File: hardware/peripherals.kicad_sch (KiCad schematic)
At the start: 32 parts, among them J6 PCM12SMTR, J7 USB_C_Receptacle_USB2.0_14P, J8 BM03B-SRSS-TB, Q4 2N7002, SW1 SW_Push, U3 74AHCT1G125, U4 DS3231MZ, U5 USBLC6-2SC6, U6 74AHCT1G32

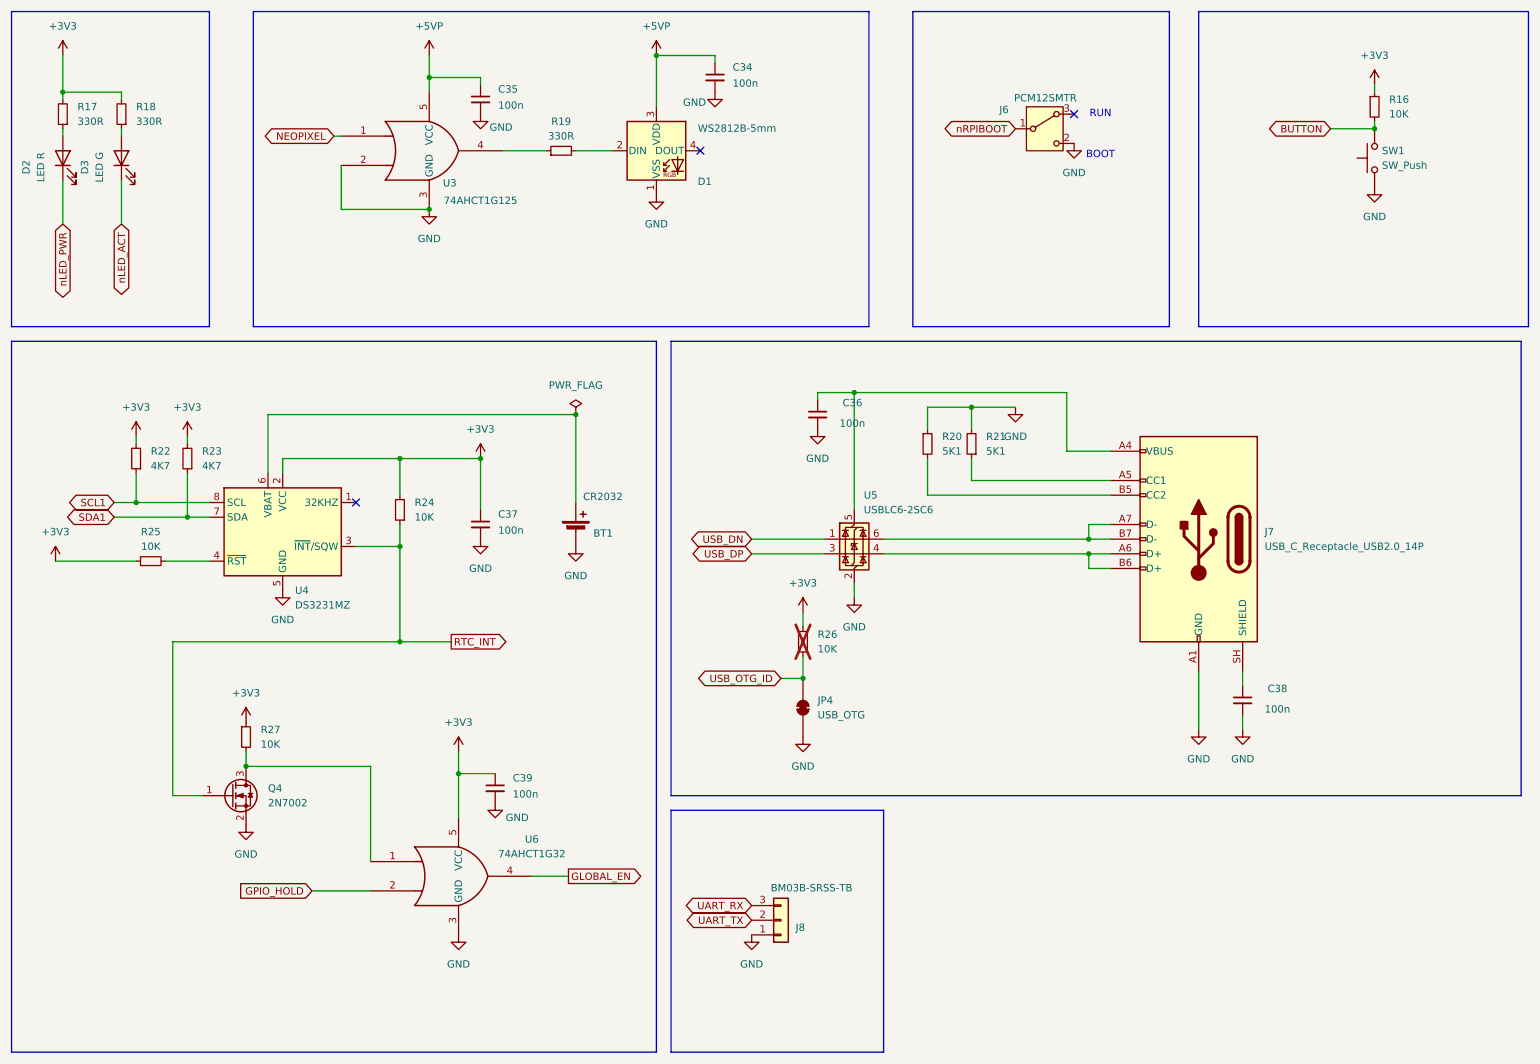
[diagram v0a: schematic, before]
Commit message: refactor: reannotate PCB by position + rename IC1 to U prefix
All reference designators renumbered top-to-bottom, left-to-right.
ASM1061 changed from IC to U prefix.
ERC: 0 errors. DRC: 0 violations. Parity: 0 issues.
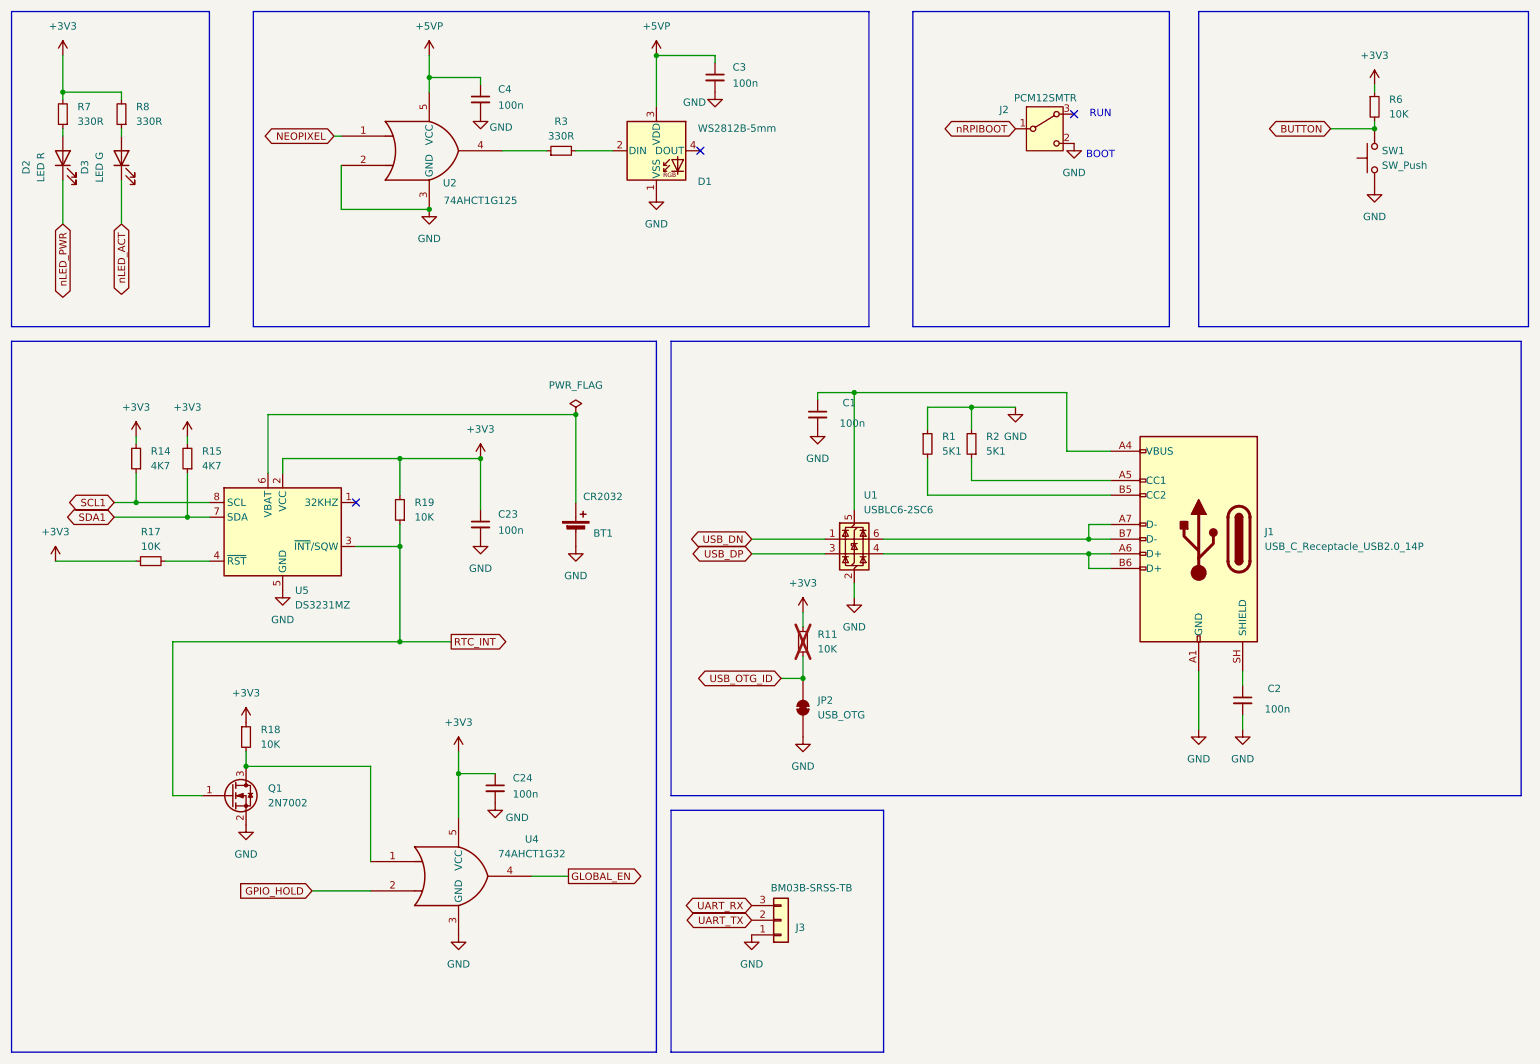
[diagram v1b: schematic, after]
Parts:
- C1: renamed from C36; KiLib_Generator (none) -> SMD_2terminal_chip_molded
- C2: renamed from C38; KiLib_Generator (none) -> SMD_2terminal_chip_molded
- C23: renamed from C37; KiLib_Generator (none) -> SMD_2terminal_chip_molded
- C24: renamed from C39; KiLib_Generator (none) -> SMD_2terminal_chip_molded
- C3: renamed from C34; KiLib_Generator (none) -> SMD_2terminal_chip_molded
- C4: renamed from C35; KiLib_Generator (none) -> SMD_2terminal_chip_molded
- D2, D3: KiLib_Generator (none) -> SMD_2terminal_chip_molded
- J3: renamed from J8; KiLib_Generator (none) -> connector/SMD_single_row_plus_mounting_pad
- Q1: renamed from Q4; KiLib_Generator (none) -> package/gullwing
- R1: renamed from R20; KiLib_Generator (none) -> SMD_2terminal_chip_molded
- R11: renamed from R26; KiLib_Generator (none) -> SMD_2terminal_chip_molded
- R14: renamed from R22; KiLib_Generator (none) -> SMD_2terminal_chip_molded
- R15: renamed from R23; KiLib_Generator (none) -> SMD_2terminal_chip_molded
- R17: renamed from R25; KiLib_Generator (none) -> SMD_2terminal_chip_molded
- R18: renamed from R27; KiLib_Generator (none) -> SMD_2terminal_chip_molded
- R19: renamed from R24; KiLib_Generator (none) -> SMD_2terminal_chip_molded
- R2: renamed from R21; KiLib_Generator (none) -> SMD_2terminal_chip_molded
- R3: renamed from R19; KiLib_Generator (none) -> SMD_2terminal_chip_molded
- R6: renamed from R16; KiLib_Generator (none) -> SMD_2terminal_chip_molded
- R7: renamed from R17; KiLib_Generator (none) -> SMD_2terminal_chip_molded
- R8: renamed from R18; KiLib_Generator (none) -> SMD_2terminal_chip_molded
- U1: renamed from U5; KiLib_Generator (none) -> package/gullwing
- U2: renamed from U3; KiLib_Generator (none) -> package/gullwing
- U4: renamed from U6; KiLib_Generator (none) -> package/gullwing
- U5: renamed from U4; KiLib_Generator (none) -> package/gullwing
- renumbered J7 to J1, J6 to J2, JP4 to JP2

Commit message: feat: add InvenTree IPN field to all schematic symbols
102 components mapped to 41 unique InvenTree part numbers.
IPN format: category prefix + sequential number (e.g. C-001, R-002, U-009).
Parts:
- BT1: IPN (none) -> BT-001
- C1, C2, C23, C24, C3, C4: IPN (none) -> C-001
- D1: IPN (none) -> D-008
- D2: IPN (none) -> D-002
- D3: IPN (none) -> D-001
- J1: IPN (none) -> J-004
- J2: IPN (none) -> J-005
- J3: IPN (none) -> J-006
- Q1: IPN (none) -> Q-003
- R1, R2: IPN (none) -> R-019
- R11, R17, R18, R19, R6: IPN (none) -> R-002
- R14, R15: IPN (none) -> R-003
- R3, R7, R8: IPN (none) -> R-018
- SW1: IPN (none) -> SW-003
- U1: IPN (none) -> U-011
- U2: IPN (none) -> U-008
- U4: IPN (none) -> U-003
- U5: IPN (none) -> U-010

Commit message: chore: remove redundant supplier fields, keep IPN as single link to InvenTree
Removed: Supplier, Digikey, Notes, KiLib_Generator, Mouser, Arrow fields.
InvenTree IPN is now the only external reference in the schematic.
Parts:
- C1, C2, C23, C24, C3, C4: Digikey 1276-1180-1-ND -> (none); KiLib_Generator SMD_2terminal_chip_molded -> (none); Notes 10% 16V Ceramic Capacitor X7R -> (none); Supplier https://www.digikey.ch/de/products/detail/samsung-electro-m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 -> (none)
- D2, D3, R1, R11, R14, R15, R17, R18, R19, R2, R3, R6, R7, R8: KiLib_Generator SMD_2terminal_chip_molded -> (none)
- J3: KiLib_Generator connector/SMD_single_row_plus_mounting_pad -> (none)
- Q1: IPN Q-003 -> (none); KiLib_Generator package/gullwing -> (none)
- U1, U2, U4, U5: KiLib_Generator package/gullwing -> (none)

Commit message: feat: complete IPN assignment for all BOM parts
All components now have InvenTree IPN field.
Added IPN to granit library symbols (ASM1061, FDS4435BZ, AP64501).
Added Q-003 to 2N7002 instances.
Only TestPoints have no IPN (not purchaseable).
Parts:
- Q1: IPN (none) -> Q-003
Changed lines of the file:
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@@
+			)
+		)
+		(property "IPN" "Q-003"
+			(at 53.34 151.13 0)
+			(hide yes)
+			(show_name no)
+			(do_not_autoplace no)
+			(effects
+				(font
+					(size 1.27 1.27)
+				)
 			)
 		)

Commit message: chore: use existing SK6812/WS2812B stock (D-007) instead of D-008
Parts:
- D1: IPN D-008 -> D-007
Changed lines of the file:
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@@
 			)
 		)
-		(property "IPN" "D-008"
+		(property "IPN" "D-007"
 			(at 0 0 0)
 			(hide yes)
